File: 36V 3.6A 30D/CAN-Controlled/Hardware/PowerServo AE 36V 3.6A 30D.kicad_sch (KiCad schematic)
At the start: 23 parts, among them J1 Control_In, J2 MOT_A, J3 Prog_IN, J4 Power_In, J6 Control_In, J7 MOT_B, U1 LMZM23601V5, U2 TLV76733DRVx, U3 DRV8871DDA, U4 MA730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

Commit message: Review Request Files and Preparations
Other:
- note added: "CAN-BUS"
- note added: "ENCODER"
- note added: "MOTOR DRIVER"
- note added: "POWER"
- note added: "uC"
- moved on the sheet: C3, C4, J3, U7

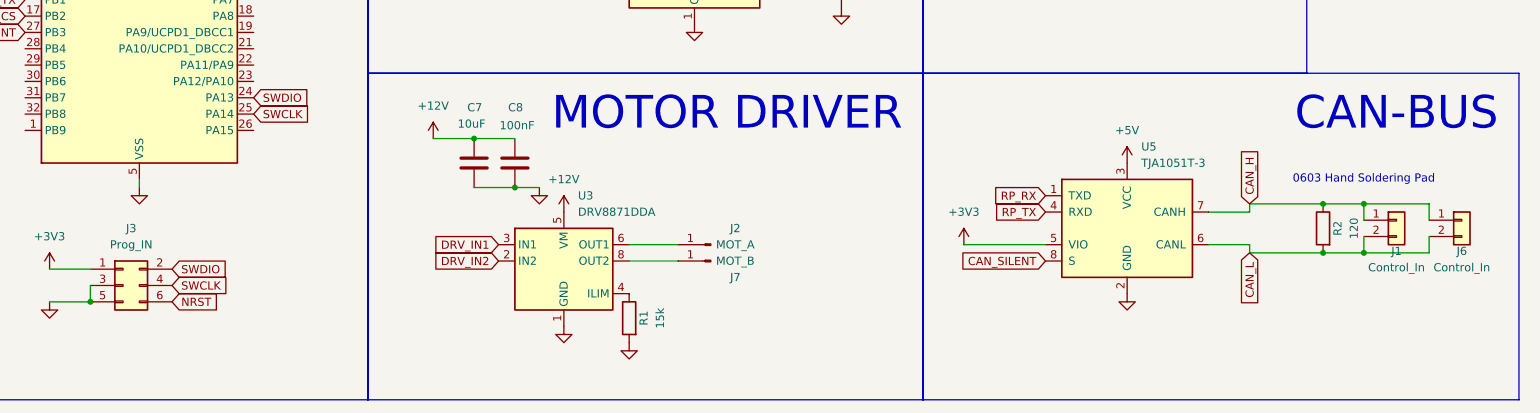
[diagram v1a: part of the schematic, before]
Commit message: Bumped to V0.7
Following Reddit Review:
- Added C10 as NRST Cap
- Added R3 as Boot0/SWCLK Pull-Down
- Added Solder Jumper for CAN Termination
-- Downscaled R2
- Fixed some of the odd orientations of components
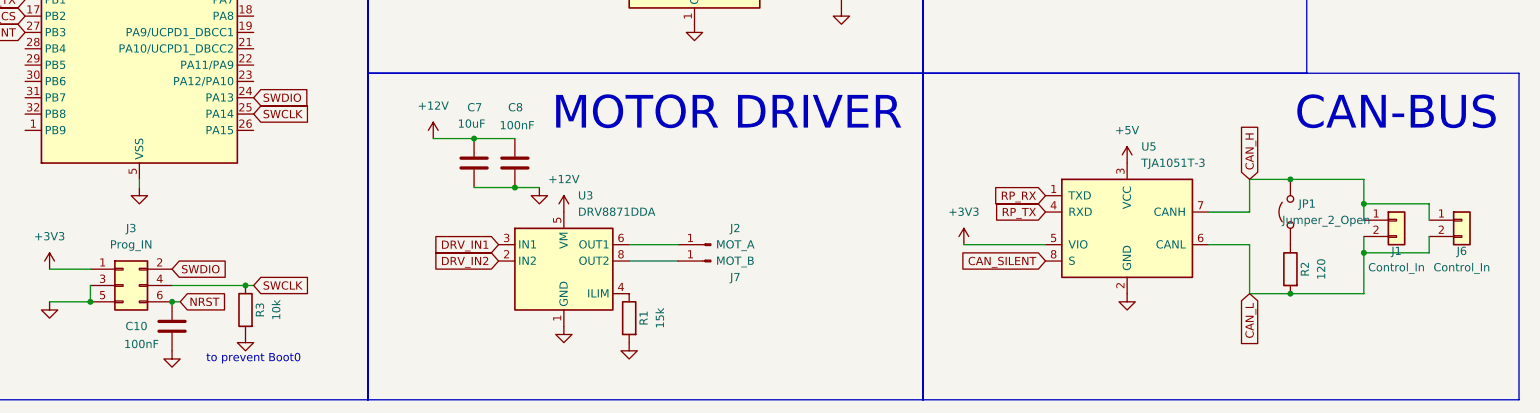
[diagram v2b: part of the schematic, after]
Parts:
- added C10: 100nF, Capacitor_SMD:C_0402_1005Metric, symbol Device:C
- added JP1: Jumper_2_Open, Jumper:SolderJumper-2_P1.3mm_Open_Pad1.0x1.5mm, symbol Jumper:Jumper_2_Open
- added R3: 10k, Resistor_SMD:R_0402_1005Metric, symbol Device:R
- R2: footprint Resistor_SMD:R_0603_1608Metric_Pad0.98x0.95mm_HandSolder -> Capacitor_SMD:C_0402_1005Metric
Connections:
- net CAN_H: now also JP1.2 (B); no longer R2.1
- net GND: now also C10.1, R3.2
- net NRST: now also C10.2
- net SWCLK: now also R3.1
- new net: JP1.1 (A), R2.1
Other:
- note added: "to prevent Boot0"
- note removed: "0603 Hand Soldering Pad"
- moved on the sheet: R2

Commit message: Finalized Reddit TODO
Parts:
- removed U3: DRV8871DDA, Package_SO:Texas_HTSOP-8-1EP_3.9x4.9mm_P1.27mm_EP2.95x4.9mm_Mask2.4x3.1mm_ThermalVias, symbol Driver_Motor:DRV8871DDA
- added C11: 100nF, Capacitor_SMD:C_0603_1608Metric, symbol Device:C
- added IC1: DRV8251DDAR, SOIC127P600X170-9N, symbol _Custom:DRV8251DDAR
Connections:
- net +12V: now also IC1.5 (VM)
- net +3V3: now also C11.2, IC1.4 (VREF)
- net DRV_IN1: now also IC1.3 (IN1)
- net DRV_IN2: now also IC1.2 (IN2)
- net GND: now also C11.1, IC1.1 (GND), IC1.9 (THERMAL_PAD)
- net at J2.1 (Pin_1): now also IC1.6 (OUT1)
- net at R1.1: now also IC1.7 (ISEN)
- net at J7.1 (Pin_1): now also IC1.8 (OUT2)
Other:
- moved on the sheet: J2, J7, R1
